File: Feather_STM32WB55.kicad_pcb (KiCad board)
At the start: 4 copper layers, 52.5 x 22.9 mm, 48 parts, among them J1 JST-SH Qwiic, J2 Conn_Battery, J3 Conn_ARM_JTAG_SWD_10, J4 Conn_Right, J5 USB_C_Receptacle_USB2.0, J6 Conn_Left, Q1 NTR4171PT1G, SW1 SMD-BUTTON-TOP-DHT-4235A_4P-4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, U1 MCP73831-2-OT, U2 AP2112K-3.3, U3 STM32WB55CGU6, U4 USBLC6-2SC6, U5 Flash SOIC-8, Y1 32Mhz

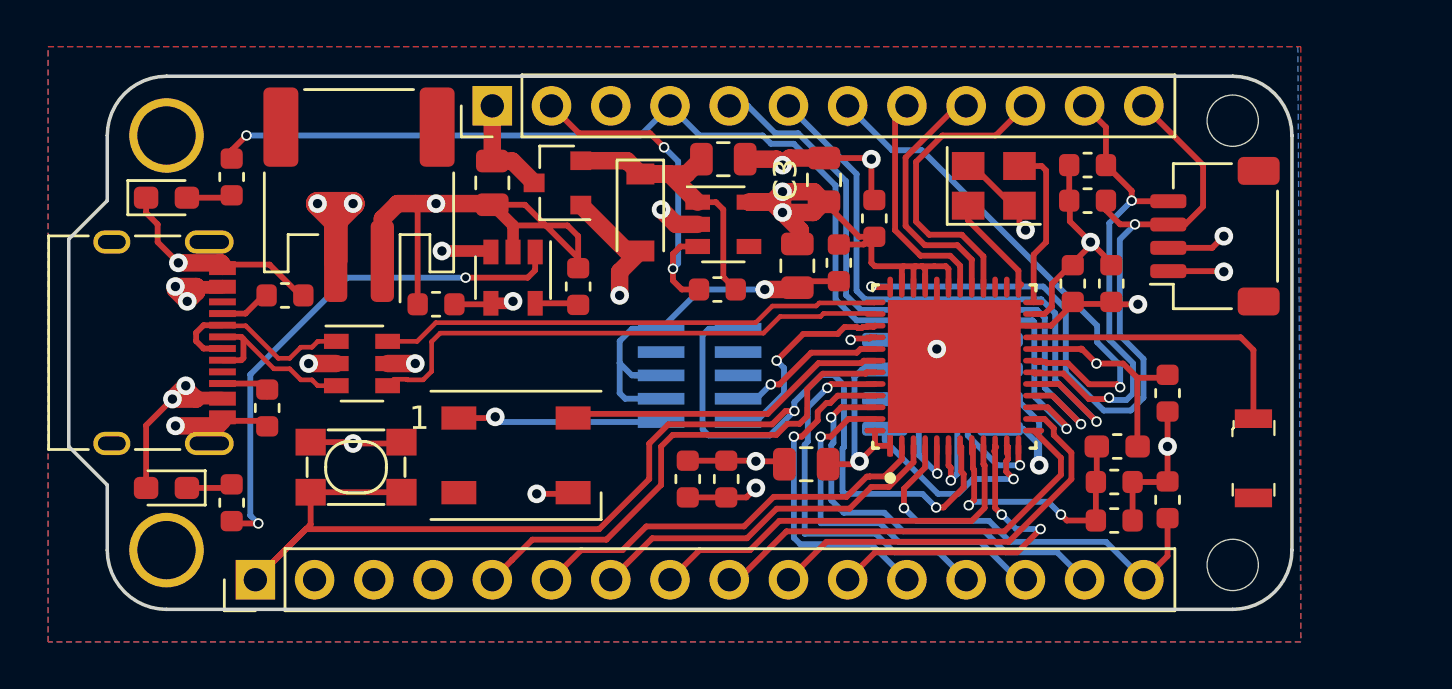
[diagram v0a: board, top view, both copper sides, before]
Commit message: Removed copper fill on F.Cu updated the PCB images
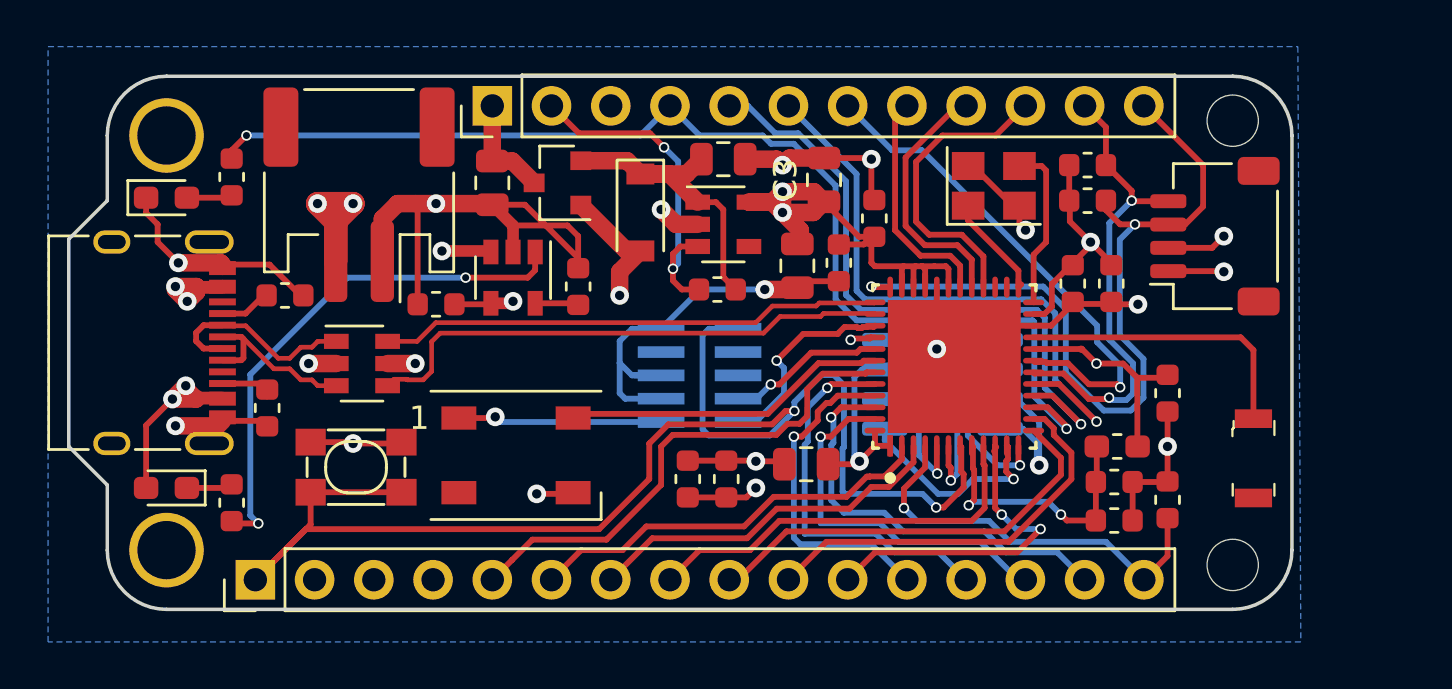
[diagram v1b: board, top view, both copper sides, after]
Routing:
- removed copper zone on F.Cu, net GND
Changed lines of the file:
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@@
-    )
-  )
-  (zone (net 58) (net_name GND) (layer F.Cu) (hatch edge 0.508)
-    (connect_pads (clearance 0.508))
-    (min_thickness 0.254)
-    (fill yes (arc_segments 32) (thermal_gap 0.508) (thermal_bridge_width 0.508))
-    (polygon
-      (pts
-        (xy 178.181 105.537) (xy 124.46 105.537) (xy 124.46 80.01) (xy 178.181 80.01)
-      )
     )
   )

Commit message: Updated with the matching network and antenna
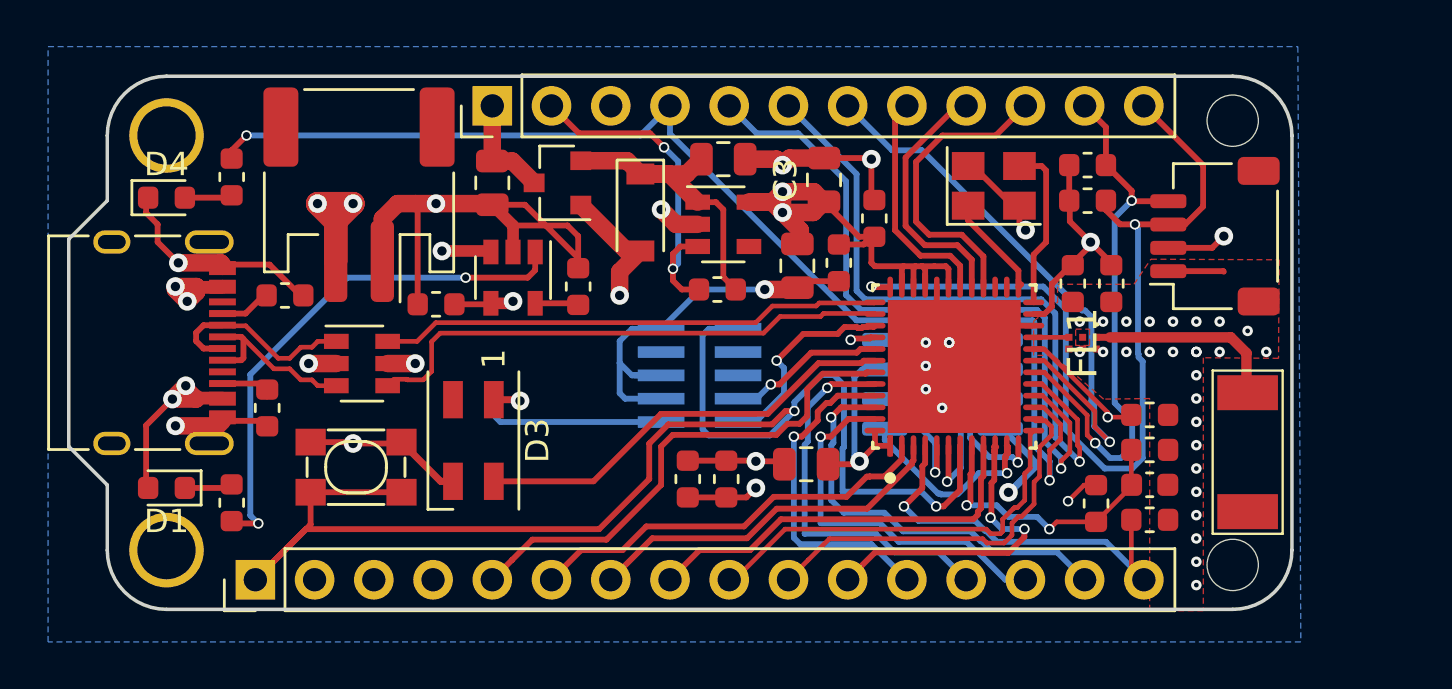
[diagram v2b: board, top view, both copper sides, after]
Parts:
- removed AE1: Fractus NN01-102, DigiKey_Footprints:Antenna_1.6x3.2mm_2450AT18A100E
- added ANT1: NN01-102, FR05S1N0102, F.Cu at (175.9, 97.4)
- added FL1: MLPF-WB55-01E3, MLPFWB5501E3, F.Cu at (168.8, 92.7)
- D1, D4: footprint LED_SMD:LED_0603_1608Metric_Pad1.05x0.95mm_HandSolder -> LED_SMD:LED_0603_1608Metric
- D3: footprint LED_SMD:LED_WS2812B_PLCC4_5.0x5.0mm_P3.2mm -> LED_SMD:LED_SK6812MINI_PLCC4_3.5x3.5mm_P1.75mm
- L1: footprint Inductor_SMD:L_0603_1608Metric_Pad1.05x0.95mm_HandSolder -> Inductor_SMD:L_0603_1608Metric
- moved L1 2.61 mm to (169.4, 99.6), turned to 90 degrees
- moved C5 2.16 mm to (171.7, 98.8)
- moved C6 2.05 mm to (171.7, 97.3)
- moved D3 1.93 mm to (142.7, 96.9), turned to 270 degrees
- moved C10 1.21 mm to (171.7, 95.8), turned to 0 degrees
- moved R10 1.15 mm to (171.7, 100.3), turned to 0 degrees
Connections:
- U3 pad 21: Net-(AE1-Pad1) -> RF_OUT
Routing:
- net Net-(AE1-Pad1): track 12.6 -> 0.00 mm
- net GND: track 102.9 -> 93.3 mm, vias 16 -> 44
- net ANT_OUT: track 0.00 -> 8.44 mm
- net D8_NEOPIXEL: track 14.0 -> 18.5 mm
- net I2C_SDA: track 35.2 -> 39.6 mm
- net I2C_SCL: track 20.5 -> 24.1 mm
- net D12: track 27.9 -> 31.1 mm
- net D10: track 22.9 -> 26.1 mm
- net D11: track 26.8 -> 29.2 mm
- net D13: track 49.2 -> 51.1 mm
- net RF_OUT: track 0.00 -> 1.52 mm
- net A4: track 18.5 -> 17.7 mm
- net +3.3VA: track 38.6 -> 39.2 mm
- net SPI_SCK: track 14.5 -> 13.8 mm
- net A5: track 17.4 -> 16.8 mm
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- added copper zone on F.Cu, net GND
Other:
- net class Default: clearance 0.2 -> 0.127; trace_width 0.25 -> 0.127
- rule trace_clearance: 0.2 -> 0.127
- rule trace_min: 0.2 -> 0.127
- rule via_min_drill: 0.3 -> 0.2
- rule via_min_size: 0.4 -> 0.45

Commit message: Updated ready for manufacturing
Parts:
- added G***: LOGO, Makeristic-KiCad-Library:stemma_qt_logo, B.Cu at (175.9, 89.0)
- SPI FLASH: renamed from U5
- moved D3 2.33 mm to (143.9, 98.9), turned to 0 degrees
- moved R8 2.30 mm to (134.0, 97.8)
- moved SW1 0.96 mm to (137.7, 99.0)
- moved R9 0.72 mm to (134.6, 91.4)
- renumbered J3 to SWD
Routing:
- net NRST: track 61.0 -> 55.5 mm
- net D8_NEOPIXEL: track 18.5 -> 16.2 mm
- net Net-(J5-PadB5): track 2.32 -> 4.26 mm
- net VBUS: track 22.5 -> 21.0 mm, vias 7 -> 9
- net GND: track 93.3 -> 91.9 mm, vias 44 -> 21
- net VDD: track 73.6 -> 75.0 mm
- net D10: track 26.1 -> 24.9 mm
- net USB_D+: track 23.0 -> 22.2 mm
- net I2C_SCL: track 24.1 -> 23.3 mm
- net USB_D-: track 21.6 -> 22.1 mm
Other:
- board text added: "Feather STM32WB55 makeristic.com"
- board text added: "RST"

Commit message: v1.1 work in progress
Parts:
- moved SPI FLASH 10.4 mm to (152.4, 94.3)
- moved C5 9.86 mm to (181.4, 97.3)
- moved C6 9.86 mm to (181.4, 95.8)
- moved R10 9.86 mm to (181.4, 98.8)
- moved C10 8.51 mm to (168.8, 87.8)
- moved SWD 7.80 mm to (144.6, 94.3)
- moved Y1 0.67 mm to (164.5, 86.4)
- moved ANT1 0.45 mm to (176.1, 97.0)
- moved R3 0.39 mm to (168.8, 86.3)
- moved R2 0.37 mm to (168.8, 84.8)
- moved C14 0.36 mm to (169.7, 90.1)
- moved J1 0.29 mm to (174.4, 87.8)
- moved C13 0.21 mm to (168.2, 90.1)
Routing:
- net VDD: track 75.0 -> 37.9 mm, vias 11 -> 8
- net NRST: track 55.5 -> 42.5 mm
- net QSPI_NSC: track 8.43 -> 21.0 mm
- net QSPI_IO1: track 5.37 -> 17.9 mm
- net SWDCLK: track 6.75 -> 17.4 mm
- net QSPI_CLK: track 7.24 -> 14.7 mm
- net SWDIO: track 8.90 -> 15.5 mm
- net (no net): track 0.00 -> 5.20 mm
- net +3.3VA: track 39.2 -> 35.5 mm
- net QSPI_IO0: track 8.83 -> 12.5 mm
- net GND: track 91.9 -> 88.2 mm, vias 21 -> 51
- net SPI_MISO: track 16.5 -> 14.2 mm
- net BOOT0: track 17.4 -> 15.3 mm
- net USART1_RX: track 16.1 -> 14.9 mm
- net D10: track 24.9 -> 23.7 mm
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
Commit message: v1.1 work in progress
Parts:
- removed G***: LOGO, Makeristic-KiCad-Library:stemma_qt_logo
- FLASH: renamed from SPI FLASH
- moved R10 26.0 mm to (155.4, 100.3), turned to 180 degrees
- moved C6 13.5 mm to (168.7, 100.3)
- moved C5 12.8 mm to (168.7, 98.8)
- moved L1 3.72 mm to (165.8, 100.3), turned to 180 degrees
- moved C8 2.54 mm to (154.2, 97.4), turned to 270 degrees
- moved C9 1.45 mm to (152.7, 97.4), turned to 270 degrees
- moved Y1 0.81 mm to (165.3, 86.5), turned to 270 degrees
- moved C7 0.37 mm to (156.6, 97.9)
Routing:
- net VDD: track 37.9 -> 54.4 mm, vias 8 -> 11
- net NRST: track 42.5 -> 50.6 mm, vias 2 -> 3
- net GND: track 88.2 -> 80.9 mm, vias 51 -> 36
- net BOOT0: track 15.3 -> 22.1 mm
- net (no net): track 5.20 -> 0.00 mm
- net QSPI_NSC: track 21.0 -> 24.3 mm
- net I2C_SCL: track 23.1 -> 26.3 mm
- net QSPI_CLK: track 14.7 -> 17.8 mm
- net HSE_OUT: track 6.42 -> 3.61 mm
- net HSE_IN: track 4.18 -> 6.92 mm
- net I2C_SDA: track 39.4 -> 36.7 mm
- net SPI_SCK: track 13.8 -> 11.4 mm
- net D10: track 23.7 -> 26.0 mm
- net D12: track 30.4 -> 28.3 mm
- net QSPI_IO1: track 17.9 -> 19.9 mm
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
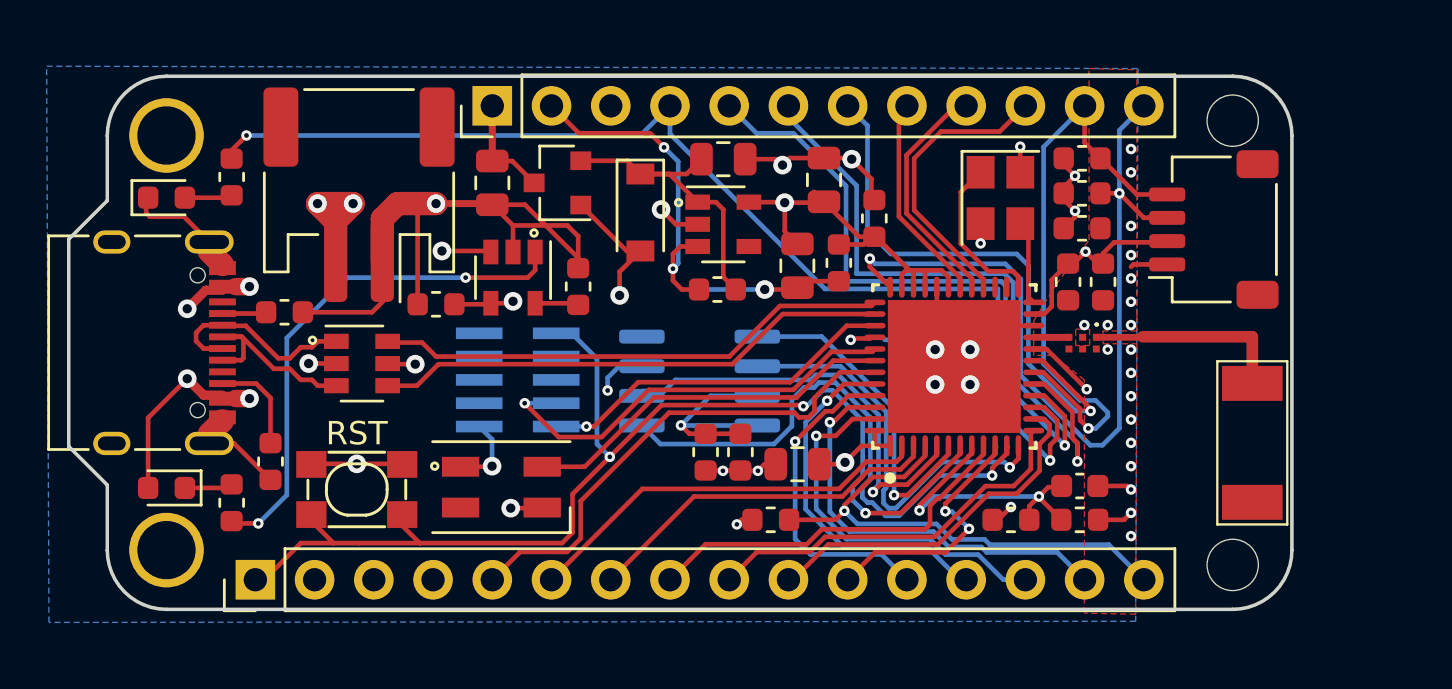
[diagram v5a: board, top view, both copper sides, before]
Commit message: Tidied up the power section, rearranged components, standardised traces to 0.3mm for power lines, 0.2mm for data lines
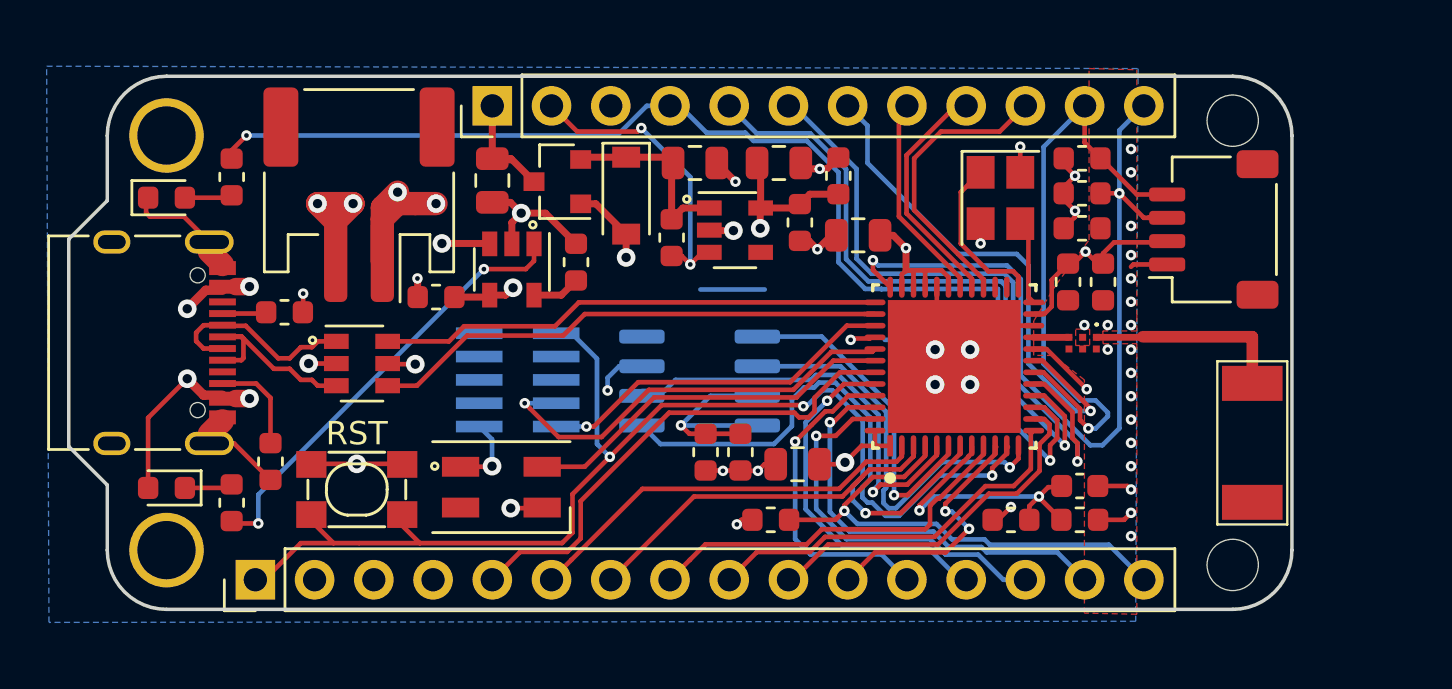
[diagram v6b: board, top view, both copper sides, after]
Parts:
- added G***: LOGO, Makeristic-KiCad-Library:stemma_qt_logo, B.Cu at (176.1, 88.7)
- moved R5 2.97 mm to (151.2, 88.2), turned to 270 degrees
- moved C4 2.92 mm to (159.2, 88.1), turned to 180 degrees
- moved C12 2.40 mm to (156.7, 87.5)
- moved C11 2.39 mm to (158.3, 85.5)
- moved C3 2.07 mm to (155.8, 85.0), turned to 0 degrees
- moved C2 1.23 mm to (152.2, 85.0)
- moved R7 1.05 mm to (147.1, 89.2)
- moved D2 0.95 mm to (149.2, 86.4)
- moved U2 0.56 mm to (153.9, 87.9)
- moved U1 0.35 mm to (144.3, 89.6)
- moved R6 0.31 mm to (141.1, 90.8)
- moved C1 0.10 mm to (143.5, 85.8)
- moved Q1 0.05 mm to (146.3, 85.8)
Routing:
- net GND: track 80.9 -> 61.6 mm, vias 36 -> 40
- net Net-(C2-Pad1): track 13.5 -> 8.36 mm
- net VDD: track 54.4 -> 50.9 mm, vias 11 -> 12
- net Net-(R1-Pad2): track 22.2 -> 19.1 mm
- net VBUS: track 19.7 -> 17.7 mm
- net D10: track 26.0 -> 24.3 mm
- net EN: track 14.7 -> 13.1 mm
- net D13: track 49.2 -> 50.8 mm
- net +BATT: track 14.2 -> 15.1 mm
- net USB_D-: track 22.1 -> 21.6 mm

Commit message: More tidying up of traces and silkscreen
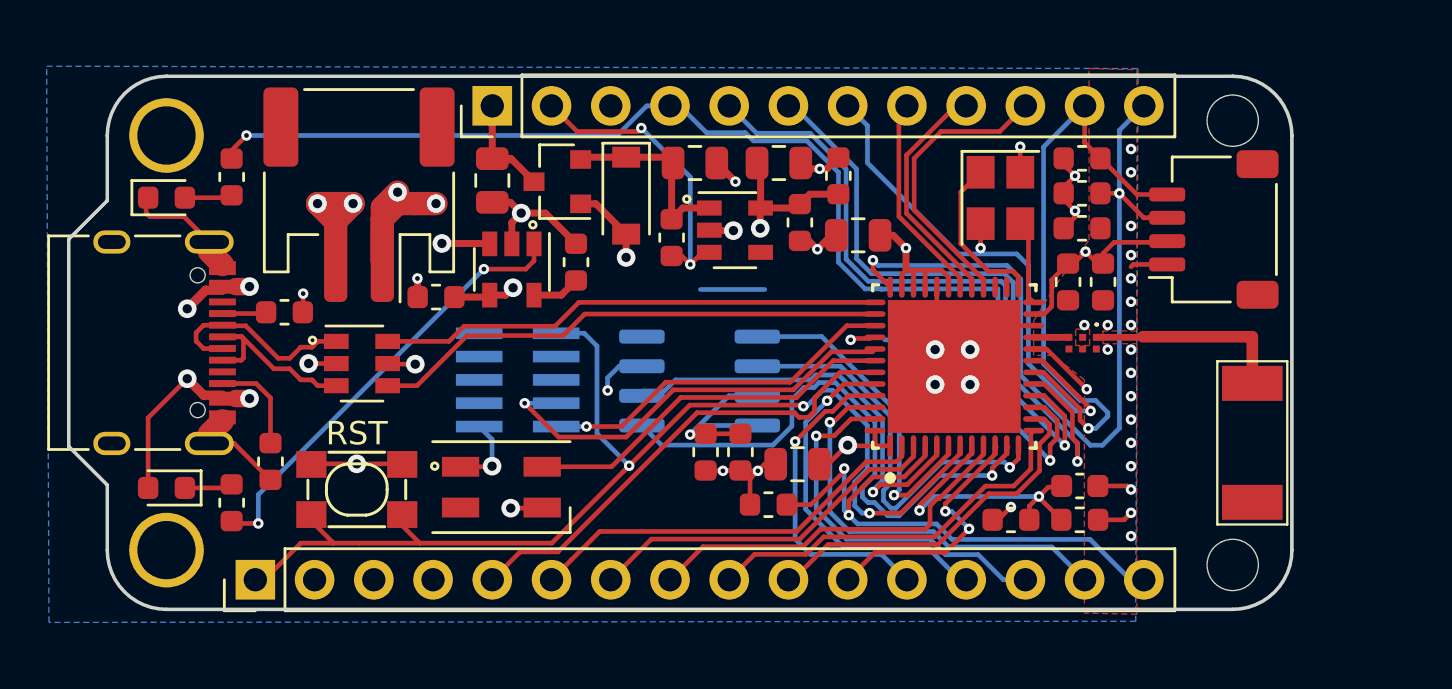
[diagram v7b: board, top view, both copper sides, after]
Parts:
- moved R10 0.66 mm to (155.3, 99.7)
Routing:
- net BOOT0: track 22.1 -> 24.4 mm, vias 1 -> 2
- net VDD: track 50.9 -> 49.8 mm
- net A0: track 21.5 -> 20.6 mm
- net GND: track 61.6 -> 62.4 mm, vias 40 -> 39

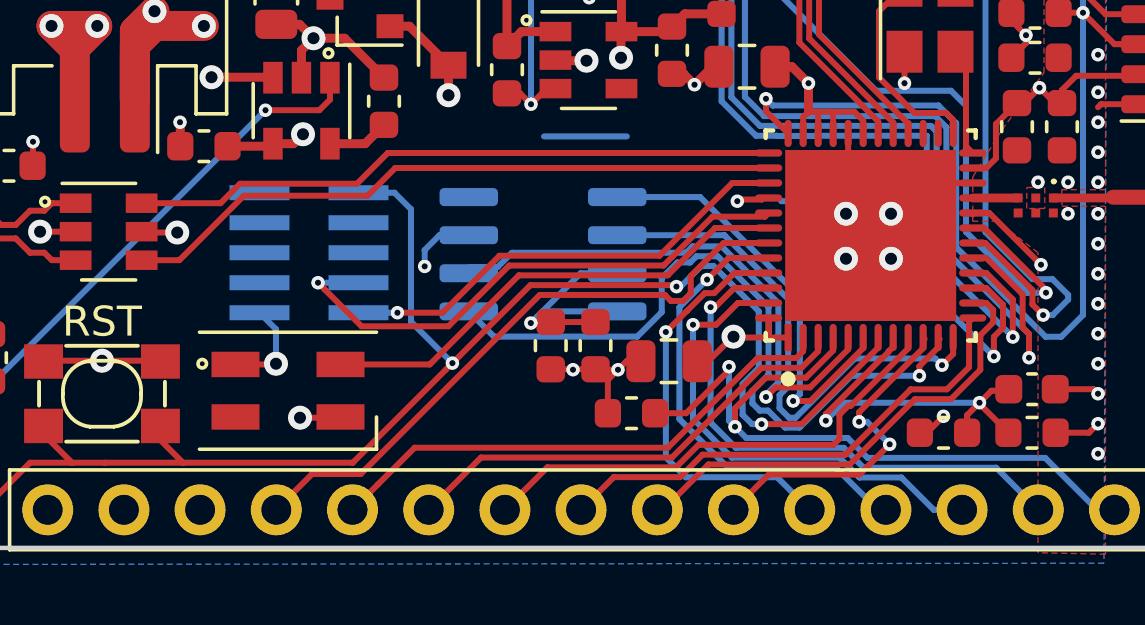
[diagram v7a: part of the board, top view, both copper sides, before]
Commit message: OCD moving traces around
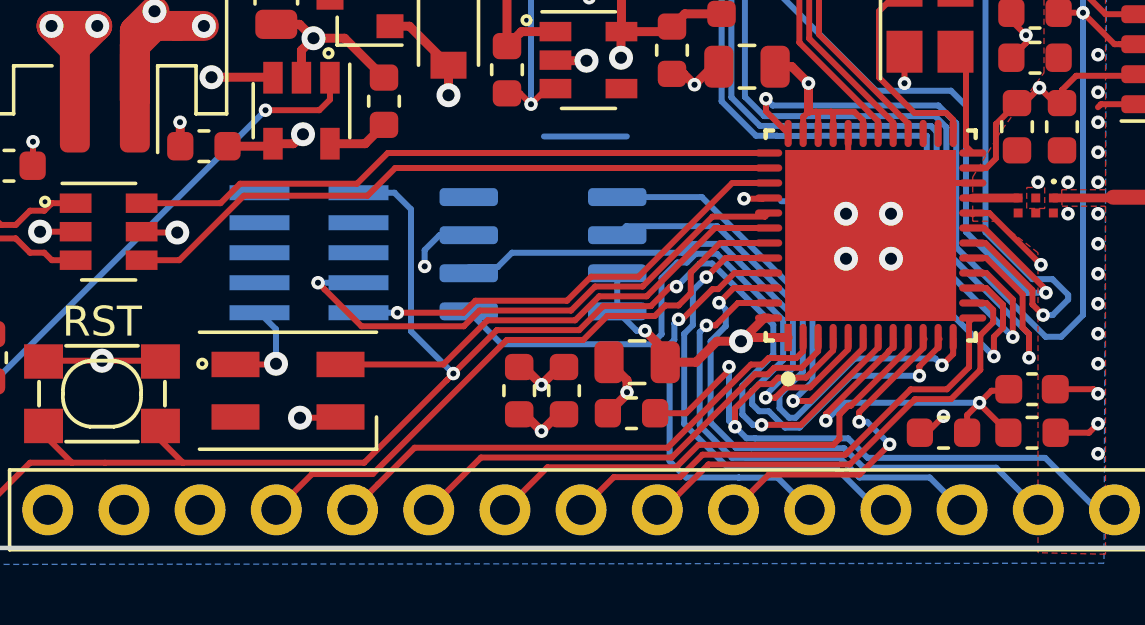
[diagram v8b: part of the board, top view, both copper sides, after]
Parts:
- moved C8 1.83 mm to (153.1, 98.9)
- moved C9 1.83 mm to (151.6, 98.9)
- moved C7 1.06 mm to (155.5, 98.0)
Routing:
- net QSPI_NSC: track 24.5 -> 25.6 mm
- net NRST: track 50.8 -> 51.7 mm
- net VDD: track 49.8 -> 49.1 mm, vias 12 -> 13
- net QSPI_CLK: track 17.9 -> 18.6 mm
- net QSPI_IO1: track 20.0 -> 20.6 mm
